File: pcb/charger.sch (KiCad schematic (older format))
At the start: 22 parts, among them J201 Conn_01x02, J202 Conn_01x02, Q201 Q_NMOS_GSD, U201 MP2359, U202 LM358, U203 MAX4377, U204 LM358

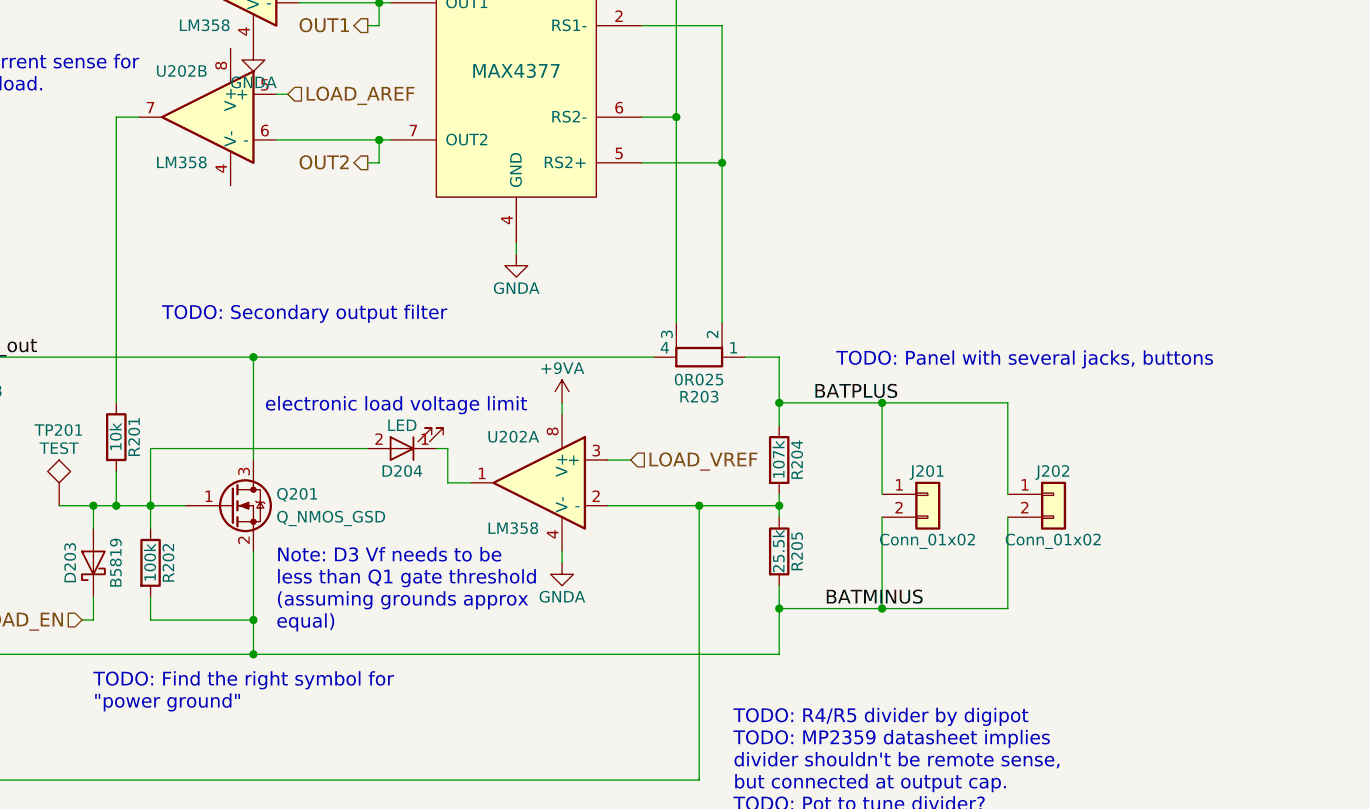
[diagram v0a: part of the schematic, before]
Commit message: Fix ERC/DRC errors for first prototype
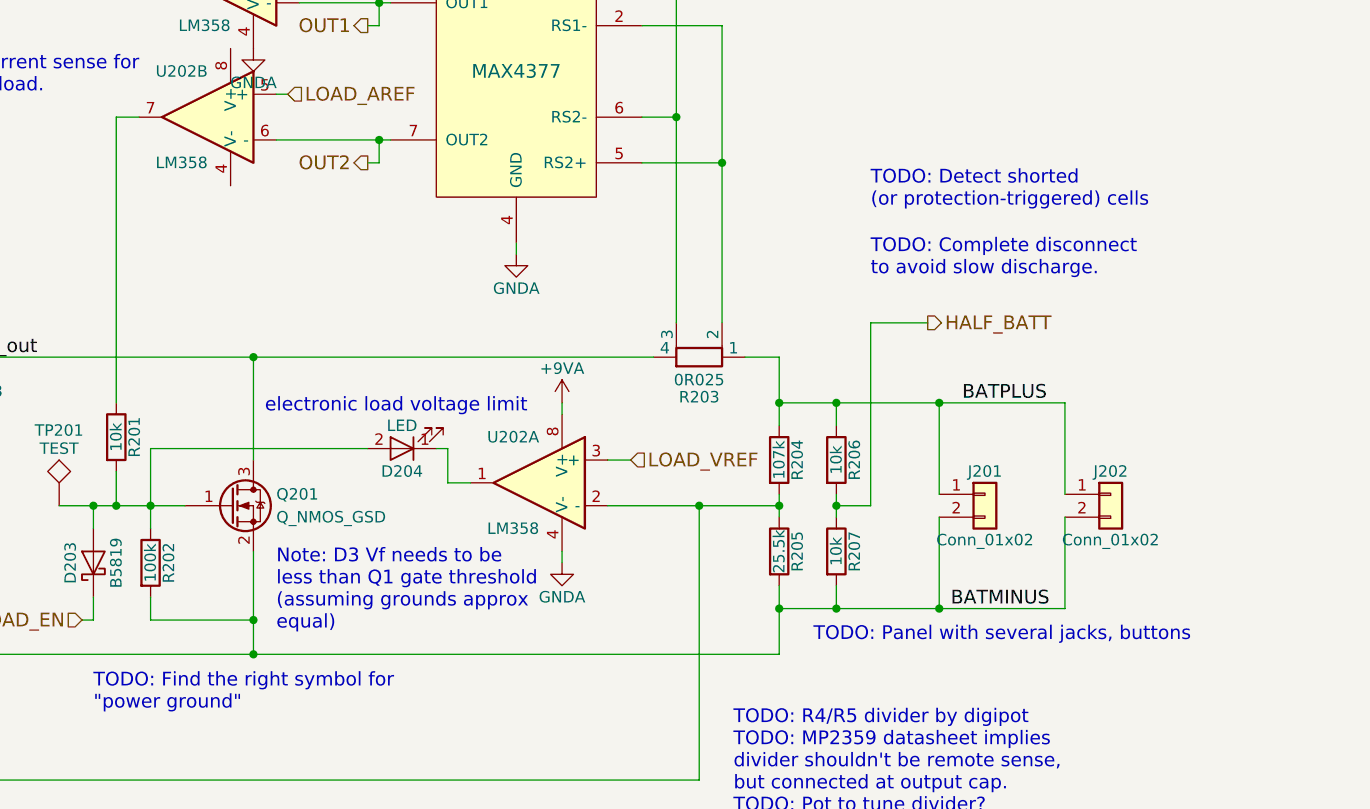
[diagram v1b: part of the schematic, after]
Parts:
- added R206, R207: 10k, Resistors_SMD:R_0603_HandSoldering, symbol R
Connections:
- net BATPLUS: now also R206.1
- net GNDIN: now also R207.2
- new net HALF_BATT: R206.2, R207.1
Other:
- note added: "TODO: Complete disconnect\nto avoid slow discharge."
- note added: "TODO: Detect shorted\n(or protection-triggered) cells"
- note removed: "TODO: Secondary output filter"
- moved on the sheet: J201, J202
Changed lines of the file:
@@
 L Conn_01x02 J201
 U 1 1 5A337C89
-P 9450 3900
-F 0 "J201" H 9450 4000 50  0000 C CNN
-F 1 "Conn_01x02" H 9450 3700 50  0000 C CNN
-F 2 "JST_Combo:JST_PH_2_Combo" H 9450 3900 50  0001 C CNN
-F 3 "" H 9450 3900 50  0001 C CNN
-	1    9450 3900
+P 9700 3900
+F 0 "J201" H 9700 4000 50  0000 C CNN
+F 1 "Conn_01x02" H 9700 3700 50  0000 C CNN
+F 2 "JST_Combo:JST_PH_2_Combo" H 9700 3900 50  0001 C CNN
+F 3 "" H 9700 3900 50  0001 C CNN
+	1    9700 3900
 	1    0    0    -1
 $EndComp
@@
 $EndComp
 $Comp
-L GND #PWR011
+L GND #PWR014
 U 1 1 5A337EA2
 P 2950 3400
-F 0 "#PWR011" H 2950 3150 50  0001 C CNN
+F 0 "#PWR014" H 2950 3150 50  0001 C CNN
 F 1 "GND" H 2950 3250 50  0000 C CNN
 F 2 "" H 2950 3400 50  0001 C CNN
@@
 Text Notes 1950 7150 0    60   ~ 0
 TODO: Add output filter with guessed component values\nhttp://www.analog.com/en/technical-articles/designing-second-stage-output-filters-for-switching-power-supplies.html
-Text Notes 9050 3350 0    60   ~ 0
+Text Notes 8950 4550 0    60   ~ 0
 TODO: Panel with several jacks, buttons
 $Comp
@@
 	1    0    0    -1
 $EndComp
-Text Notes 6100 3150 0    60   ~ 0
-TODO: Secondary output filter
 Text Notes 2350 3800 0    60   ~ 0
 TODO: Soft-start cap?
@@
 L Conn_01x02 J202
 U 1 1 5A37E853
-P 10000 3900
-F 0 "J202" H 10000 4000 50  0000 C CNN
-F 1 "Conn_01x02" H 10000 3700 50  0000 C CNN
-F 2 "Connectors_JST:JST_VH_B2PS-VH_2x2x3.96mm_Horizontal" H 10000 3900 50  0001 C CNN
-F 3 "" H 10000 3900 50  0001 C CNN
-	1    10000 3900
+P 10250 3900
+F 0 "J202" H 10250 4000 50  0000 C CNN
+F 1 "Conn_01x02" H 10250 3700 50  0000 C CNN
+F 2 "Connectors_JST:JST_VH_B2PS-VH_2x2x3.96mm_Horizontal" H 10250 3900 50  0001 C CNN
+F 3 "" H 10250 3900 50  0001 C CNN
+	1    10250 3900
 	1    0    0    -1
 $EndComp
@@
 LOAD_VREF
 $Comp
-L +9VA #PWR012
+L +9VA #PWR015
 U 1 1 5A3CAA23
 P 6500 1250
-F 0 "#PWR012" H 6500 1125 50  0001 C CNN
+F 0 "#PWR015" H 6500 1125 50  0001 C CNN
 F 1 "+9VA" H 6500 1400 50  0000 C CNN
 F 2 "" H 6500 1250 50  0001 C CNN
@@
 OUT2
 $Comp
-L +9VA #PWR014
+L +9VA #PWR016
 U 1 1 5A3CC14E
 P 7650 950
-F 0 "#PWR014" H 7650 825 50  0001 C CNN
+F 0 "#PWR016" H 7650 825 50  0001 C CNN
 F 1 "+9VA" H 7650 1100 50  0000 C CNN
 F 2 "" H 7650 950 50  0001 C CNN
@@
 $EndComp
 $Comp
-L +9VA #PWR015
+L +9VA #PWR017
 U 1 1 5A3CC759
 P 7850 3500
-F 0 "#PWR015" H 7850 3375 50  0001 C CNN
+F 0 "#PWR017" H 7850 3375 50  0001 C CNN
 F 1 "+9VA" H 7850 3650 50  0000 C CNN
 F 2 "" H 7850 3500 50  0001 C CNN
@@
 $EndComp
 $Comp
-L GNDA #PWR016
+L GNDA #PWR018
 U 1 1 5A3CC893
 P 7850 4200
-F 0 "#PWR016" H 7850 3950 50  0001 C CNN
+F 0 "#PWR018" H 7850 3950 50  0001 C CNN
 F 1 "GNDA" H 7850 4050 50  0000 C CNN
 F 2 "" H 7850 4200 50  0001 C CNN
@@
 	6700 1750 7100 1750
 Wire Wire Line
-	9250 3900 9250 3500
-Wire Wire Line
-	8800 3500 9800 3500
+	9500 3500 9500 3900
+Wire Wire Line
+	8800 3500 10050 3500
 Connection ~ 8800 3500
 Wire Wire Line
@@
 	2400 4600 8800 4600
 Wire Wire Line
-	9250 4000 9250 4400
-Wire Wire Line
-	8800 4400 9800 4400
+	9500 4400 9500 4000
+Wire Wire Line
+	8800 4400 10050 4400
 Connection ~ 8800 4400
 Connection ~ 8800 3950
@@
 	8200 1000 8200 1050
 Wire Wire Line
-	9800 3500 9800 3900
-Connection ~ 9250 3500
-Wire Wire Line
-	9800 4400 9800 4000
-Connection ~ 9250 4400
+	10050 3500 10050 3900
+Connection ~ 9500 3500
+Wire Wire Line
+	10050 4400 10050 4000
+Connection ~ 9500 4400
 Wire Wire Line
 	8050 3750 8150 3750
@@
 Wire Wire Line
 	5800 4450 5800 4350
-Text Label 8950 3500 0    60   ~ 0
+Text Label 9600 3500 0    60   ~ 0
 BATPLUS
-Text Label 9000 4400 0    60   ~ 0
+Text Label 9550 4400 0    60   ~ 0
 BATMINUS
 $Comp
@@
 Ind_out
 $Comp
-L GNDA #PWR017
+L GNDA #PWR019
 U 1 1 5A3D46AB
 P 7650 2850
-F 0 "#PWR017" H 7650 2600 50  0001 C CNN
+F 0 "#PWR019" H 7650 2600 50  0001 C CNN
 F 1 "GNDA" H 7650 2700 50  0000 C CNN
 F 2 "" H 7650 2850 50  0001 C CNN
@@
 $EndComp
 $Comp
-L GNDA #PWR018
+L GNDA #PWR020
 U 1 1 5A3D494B
 P 8200 1350
-F 0 "#PWR018" H 8200 1100 50  0001 C CNN
+F 0 "#PWR020" H 8200 1100 50  0001 C CNN
 F 1 "GNDA" H 8200 1200 50  0000 C CNN
 F 2 "" H 8200 1350 50  0001 C CNN
@@
 $EndComp
 $Comp
-L GNDA #PWR?
+L GNDA #PWR021
 U 1 1 5A3D4EF5
 P 6500 1950
-F 0 "#PWR?" H 6500 1700 50  0001 C CNN
+F 0 "#PWR021" H 6500 1700 50  0001 C CNN
 F 1 "GNDA" H 6500 1800 50  0000 C CNN
 F 2 "" H 6500 1950 50  0001 C CNN
@@
 	1    0    0    -1
 $EndComp
+$Comp
+L R R206
+U 1 1 5A3D5E6F
+P 9050 3750
+F 0 "R206" V 9130 3750 50  0000 C CNN
+F 1 "10k" V 9050 3750 50  0000 C CNN
+F 2 "Resistors_SMD:R_0603_HandSoldering" V 8980 3750 50  0001 C CNN
+F 3 "" H 9050 3750 50  0001 C CNN
+	1    9050 3750
+	1    0    0    -1
+$EndComp
+$Comp
+L R R207
+U 1 1 5A3D5ECD
+P 9050 4150
+F 0 "R207" V 9130 4150 50  0000 C CNN
+F 1 "10k" V 9050 4150 50  0000 C CNN
+F 2 "Resistors_SMD:R_0603_HandSoldering" V 8980 4150 50  0001 C CNN
+F 3 "" H 9050 4150 50  0001 C CNN
+	1    9050 4150
+	1    0    0    -1
+$EndComp
+Wire Wire Line
+	9050 4300 9050 4400
+Connection ~ 9050 4400
+Wire Wire Line
+	9050 3900 9050 4000
+Wire Wire Line
+	9050 3600 9050 3500
+Connection ~ 9050 3500
+Wire Wire Line
+	9050 3950 9200 3950
+Wire Wire Line
+	9200 3950 9200 3150
+Wire Wire Line
+	9200 3150 9450 3150
+Connection ~ 9050 3950
+Text HLabel 9450 3150 2    60   Output ~ 0
+HALF_BATT
+Text Notes 9200 2950 0    60   ~ 0
+TODO: Complete disconnect\nto avoid slow discharge.
+Text Notes 9200 2650 0    60   ~ 0
+TODO: Detect shorted\n(or protection-triggered) cells
 $EndSCHEMATC

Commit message: Massive rework, fully routed
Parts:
- removed C201: 10u, Capacitors_SMD_Round:C_1206, symbol C
- removed C203: 22u, Capacitors_SMD_Round:C_1206, symbol C
- removed D202: B230A, Diodes_SMD:D_SMA, symbol D_Schottky
- removed D203: B5819, Diodes_SMD:D_SOD-323_HandSoldering, symbol D_Schottky
- removed D204: LED, LEDs:LED_0805_HandSoldering, symbol LED
- removed L201: 4.7uH, Inductors_SMD:L_Taiyo-Yuden_NR-50xx, symbol L
- removed Q201: Q_NMOS_GSD, TO_Combo_Packages:TO_220_247, symbol Q_NMOS_GSD
- removed R201, R206, R207: 10k, Resistors_SMD:R_0603_HandSoldering, symbol R
- removed R202: 100k, Resistors_SMD:R_0603_HandSoldering, symbol R
- removed R204: 107k, Resistors_SMD:R_0603_HandSoldering, symbol R
- removed R205: 25.5k, Resistors_SMD:R_0603_HandSoldering, symbol R
- removed TP201: TEST, Measurement_Points:Measurement_Point_Round-SMD-Pad_Small, symbol TEST
- removed U201: MP2359, TO_SOT_Packages_SMD:SOT-23-6_Handsoldering, symbol MP2359
- removed U202: LM358, Housings_SOIC:SOIC-8_3.9x4.9mm_Pitch1.27mm, symbol LM358
- added unit 2 of U201
- C202: value 10n -> 0.1u
- renumbered C204 to C201, R203 to R201, U204 to U201, U203 to U202
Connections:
- net Vsw is gone; now on net GNDA: C202.2
- net +9VA: now also C202.1, U201.8 (V+)
- net GNDA: now also U201.4 (V-), U201.5 (+), U201.6 (-)
- net buck/FB: now reaches D201.1 (K)
- net Ind_out renamed output_disconnect/BATT
- no-connect marks 0 -> 1
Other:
- note added: "TODO: 2S+ charging with 4.2*n ref, feedback\nTODO: digipot for fine tune"
- note added: "TODO: Find sth fun to do with this."
- note removed: "Note: D3 Vf needs to be\nless than Q1 gate threshold\n(assuming grounds approx\nequal)"
- note removed: "OUT1 is current limit for\ncharging."
- note removed: "OUT2 is current sense for\nelectronic load."
- note removed: "TODO: Complete disconnect\nto avoid slow discharge."
- note removed: "TODO: Detect shorted\n(or protection-triggered) cells"
- note removed: "TODO: Find the right symbol for\n"power ground""
- note removed: "TODO: R4/R5 divider by digipot\nTODO: MP2359 datasheet implies\ndivider shouldn't be remote sense,\nbut connected at output cap.\nTODO: Pot to tune divider?"
- note removed: "electronic load voltage limit"
- moved on the sheet: C201, D201, J201, J202, R201, U201A, U202

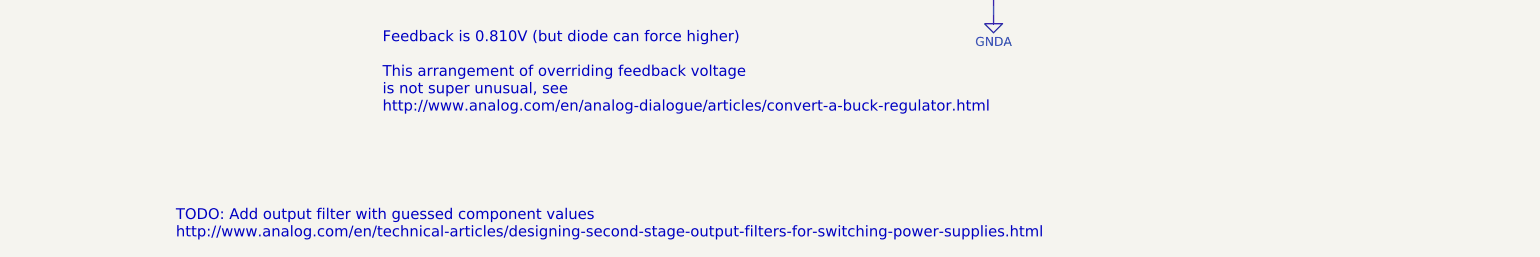
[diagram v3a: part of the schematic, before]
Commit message: Fixup url and add license
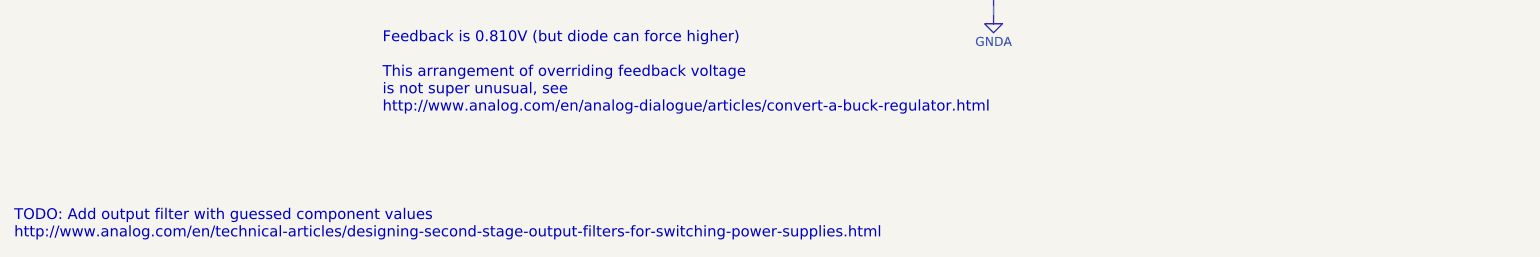
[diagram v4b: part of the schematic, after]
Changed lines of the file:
@@
 Date ""
 Rev ""
-Comp ""
-Comment1 ""
+Comp "(c) Google LLC"
+Comment1 "CC-BY 4.0 International"
 Comment2 ""
 Comment3 ""
@@
 	-1   0    0    -1
 $EndComp
-Text Notes 1950 7150 0    60   ~ 0
+Text Notes 1050 7150 0    60   ~ 0
 TODO: Add output filter with guessed component values\nhttp://www.analog.com/en/technical-articles/designing-second-stage-output-filters-for-switching-power-supplies.html
 Text Notes 8400 1950 0    60   ~ 0
